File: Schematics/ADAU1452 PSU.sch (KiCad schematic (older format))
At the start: 59 parts, among them P301 CONN_2x1, P302 CONN_2x1, P303 PIN, P304 PIN, P305 PIN, P306 PIN, U301 IC-REG-XRP7659ISTR-F, U302 IC-REG-XRP7659ISTR-F, U304 IC-REG-XC6210B332MR, U305 IC-REG-XC6210B332MR

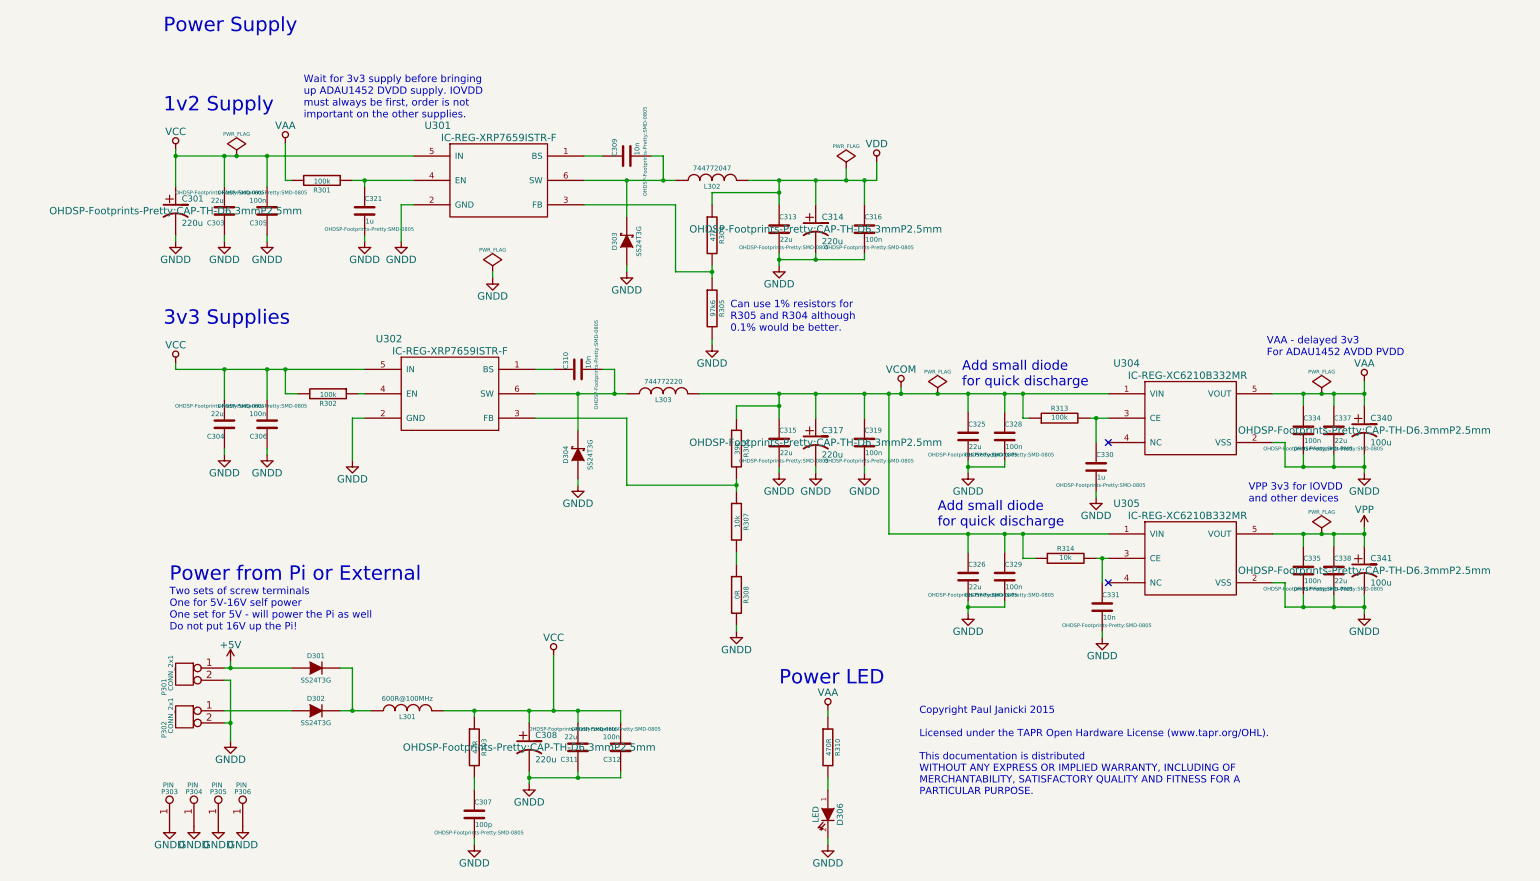
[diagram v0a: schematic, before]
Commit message: WIP
Add master audio clock to I2S headers.
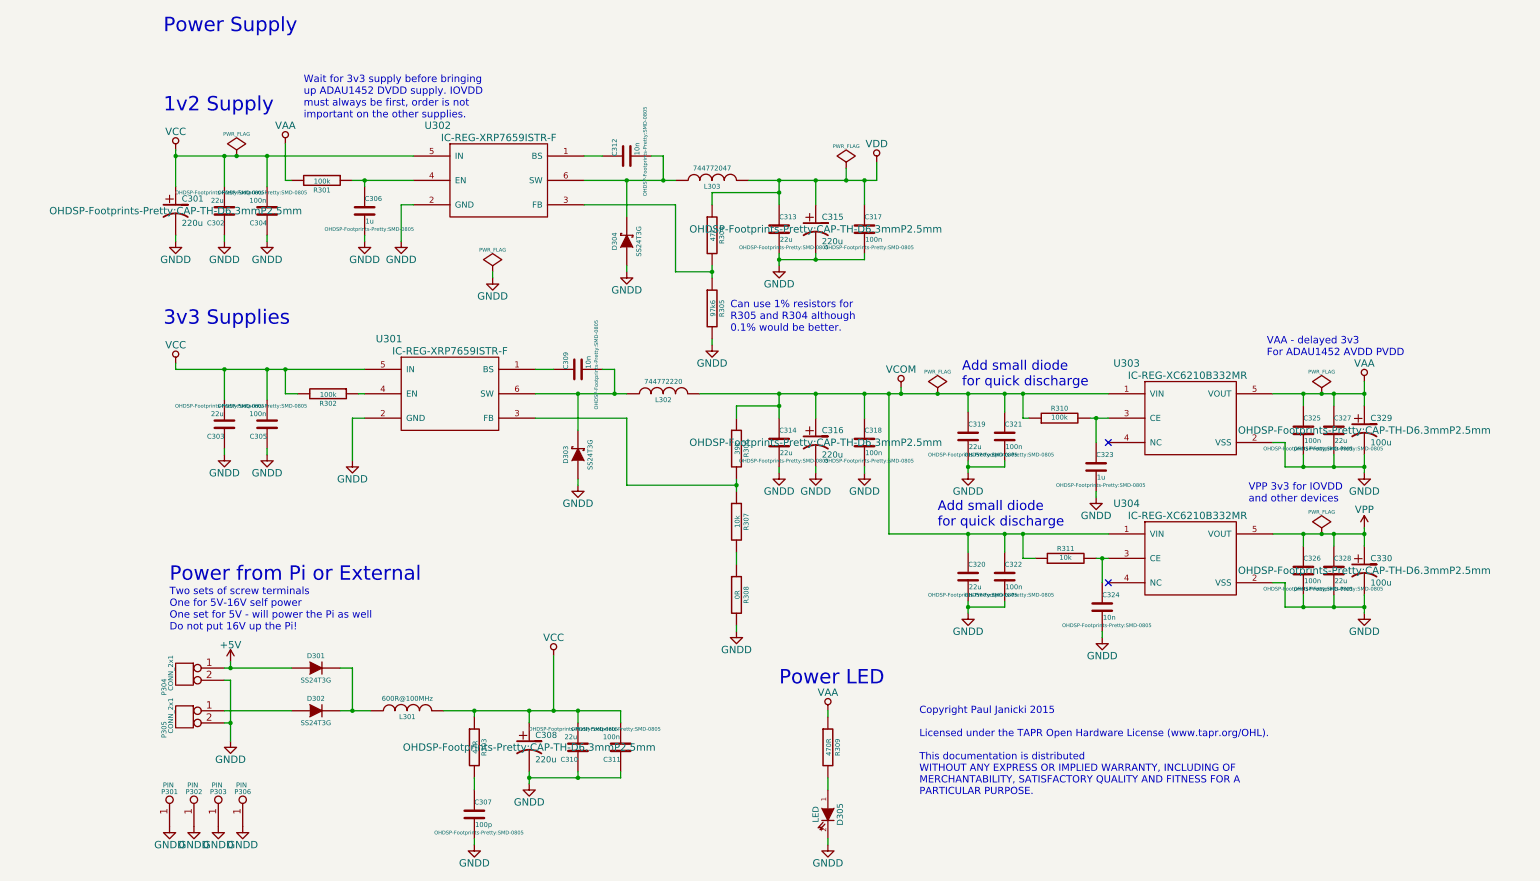
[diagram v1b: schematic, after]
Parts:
- renumbered C303 to C302, C304 to C303, C305 to C304, C306 to C305, C321 to C306, C310 to C309, C311 to C310, C312 to C311, C309 to C312, C315 to C314, C314 to C315, C317 to C316, C316 to C317, C319 to C318, C325 to C319, C326 to C320, C328 to C321, C329 to C322, C330 to C323, C331 to C324, C334 to C325, C335 to C326, C337 to C327, C338 to C328, C340 to C329, C341 to C330, D304 to D303, D303 to D304, D306 to D305, L303 to L302, L302 to L303, P303 to P301, P304 to P302, P305 to P303, P301 to P304, P302 to P305, R310 to R309, R313 to R310, R314 to R311, U302 to U301, U301 to U302, U304 to U303, U305 to U304

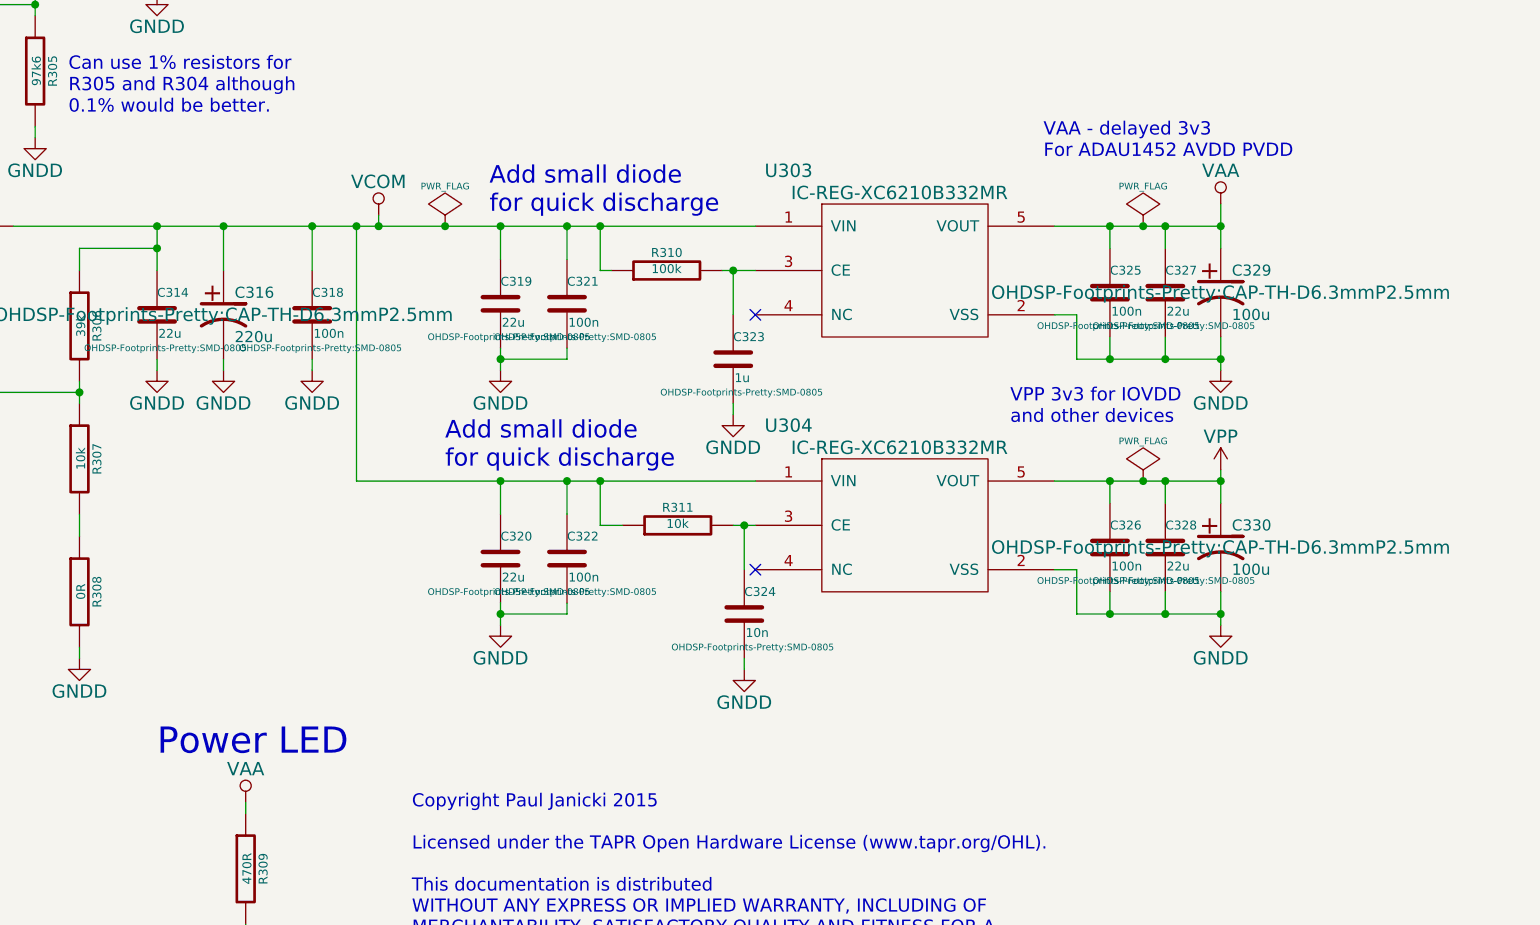
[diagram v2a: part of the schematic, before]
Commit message: WIP
Simplify PSU
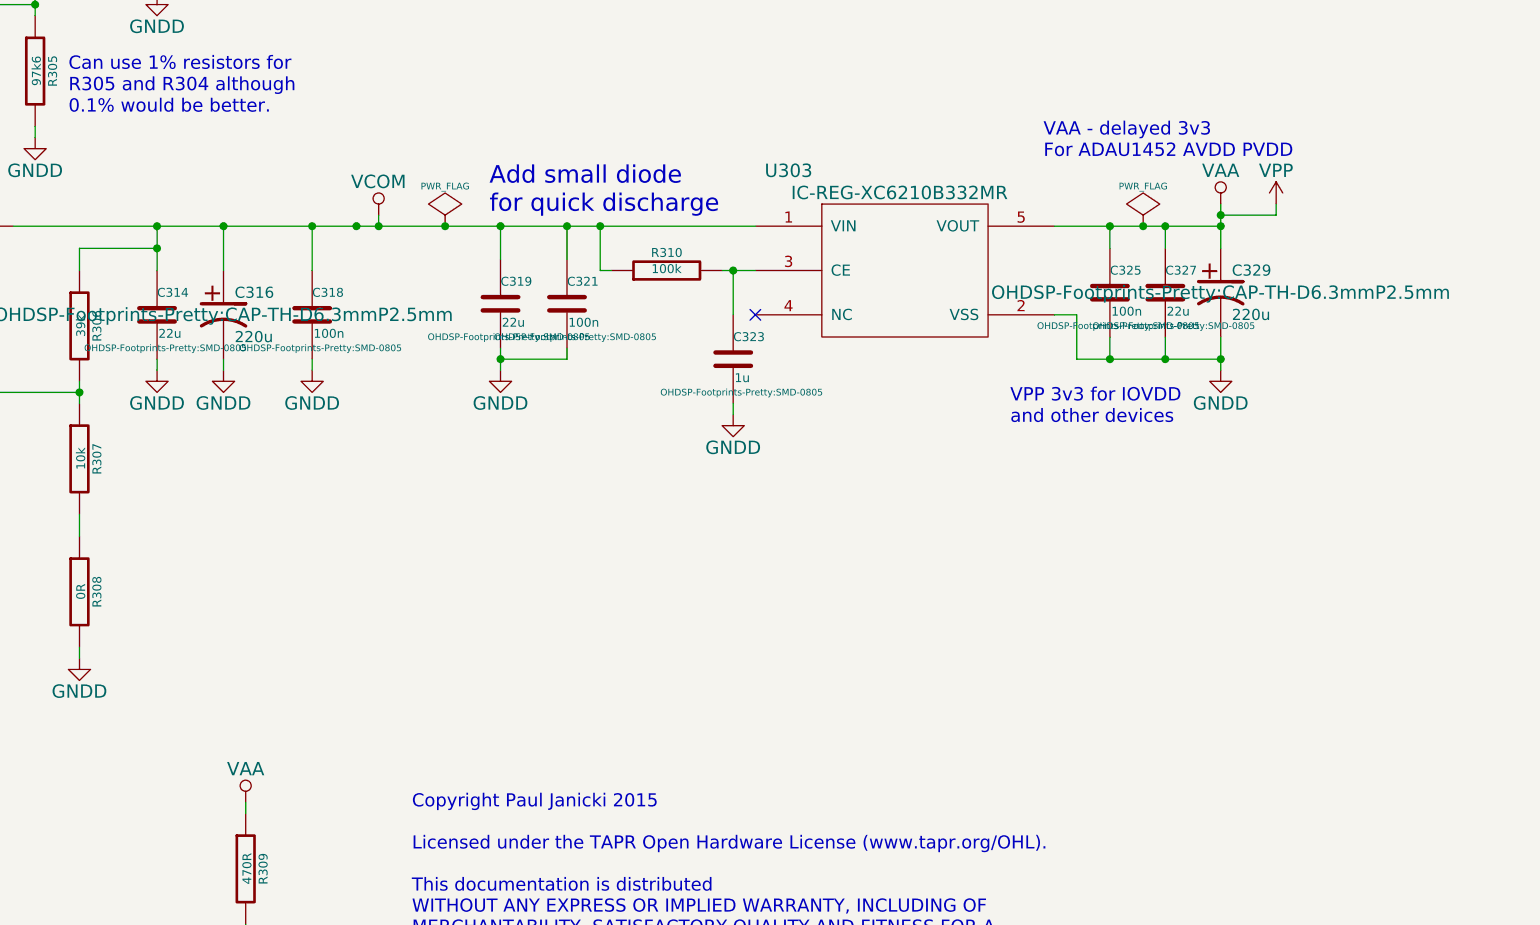
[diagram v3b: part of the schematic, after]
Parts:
- removed C320, C328: 22u, OHDSP-Footprints-Pretty:SMD-0805, symbol C
- removed C322, C326: 100n, OHDSP-Footprints-Pretty:SMD-0805, symbol C
- removed C324: 10n, OHDSP-Footprints-Pretty:SMD-0805, symbol C
- removed C330: 100u, OHDSP-Footprints-Pretty:CAP-TH-D6.3mmP2.5mm, symbol CP1
- removed R311: 10k, OHDSP-Footprints-Pretty:SMD-0805, symbol R
- removed U304: IC-REG-XC6210B332MR, OHDSP-Footprints-Pretty:IC-SOT25, symbol IC-REG-XC6210B332MR
- C329: value 100u -> 220u
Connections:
- no-connect marks 2 -> 1
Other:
- note removed: "Power LED"
